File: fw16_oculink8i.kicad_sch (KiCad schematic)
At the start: 18 parts, among them J1 173162-0131, J3 Fan0, J4 Fan1, U1 BR24G32FVT-3GE2

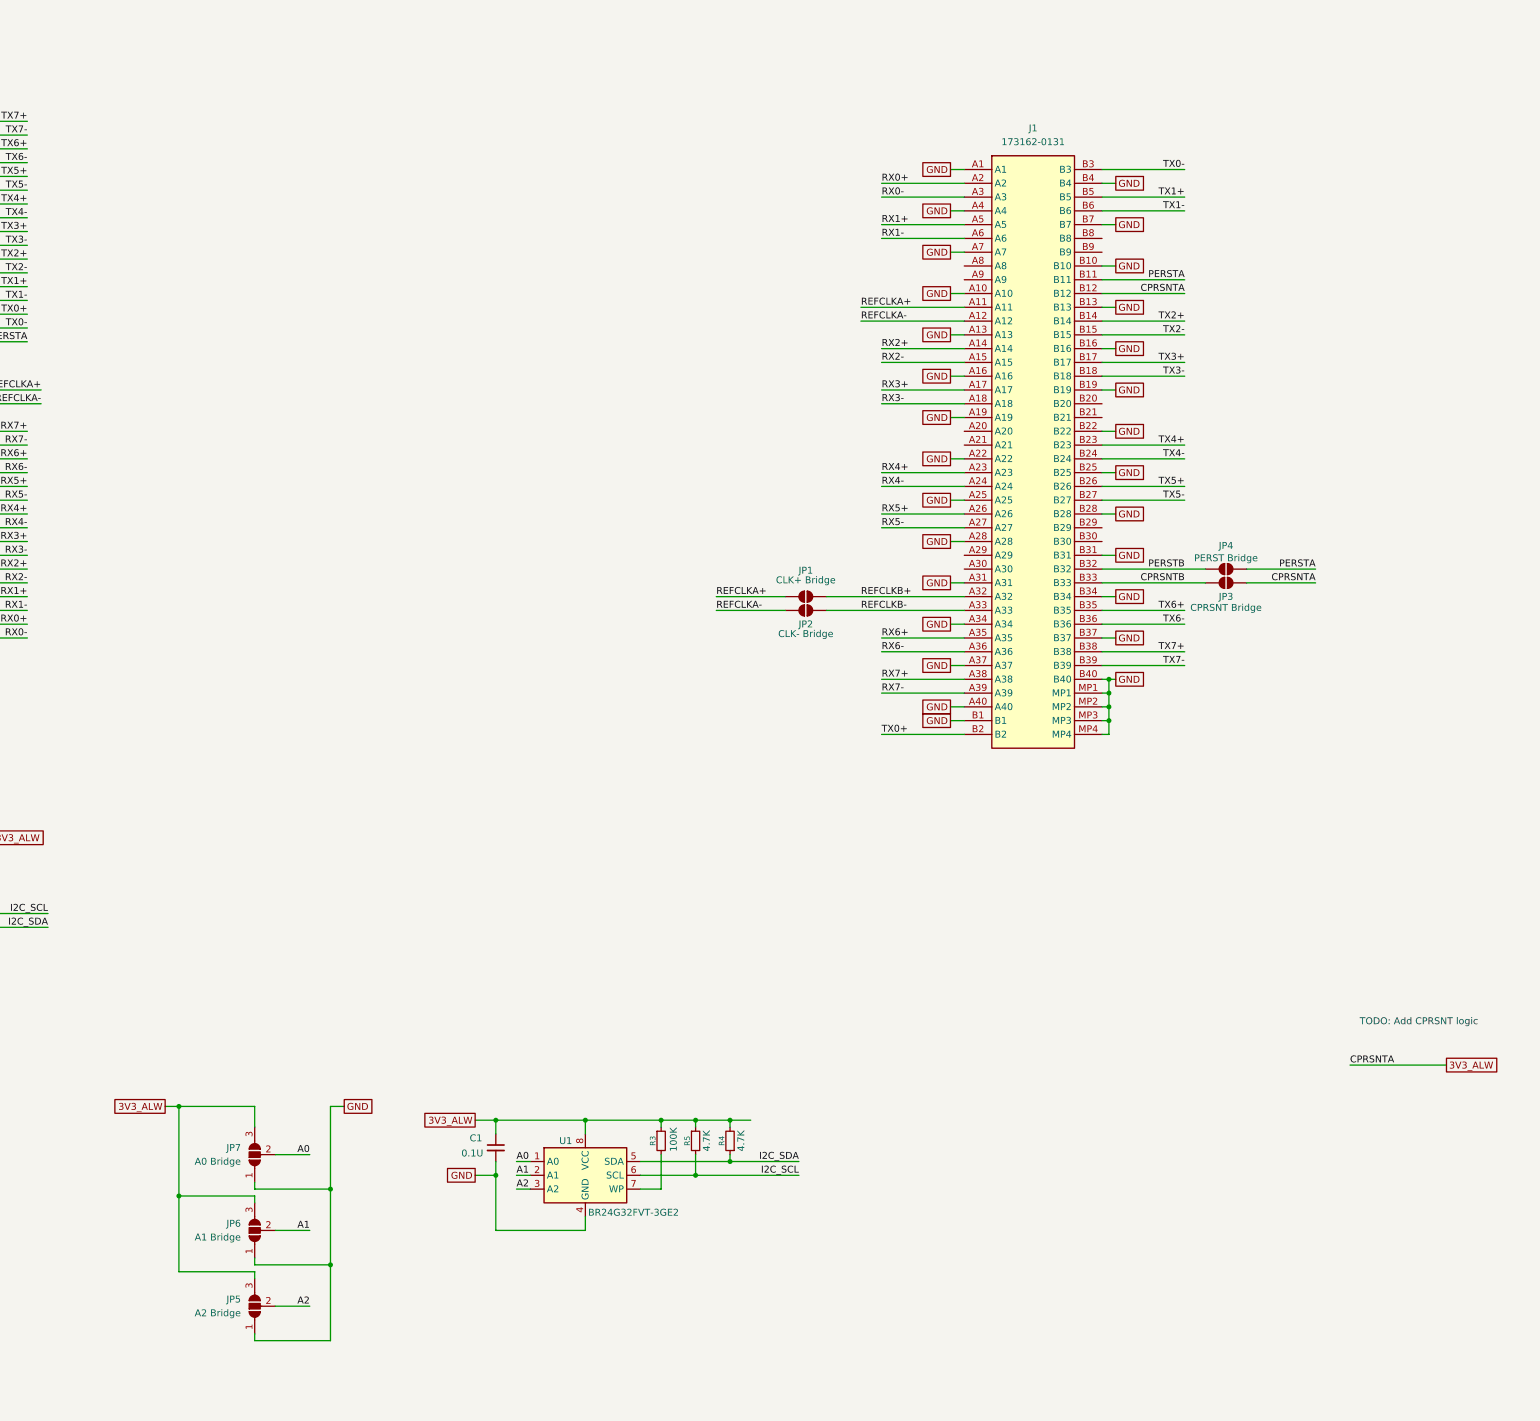
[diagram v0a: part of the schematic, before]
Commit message: Switch to 0R resistor rather than jumper solder pads
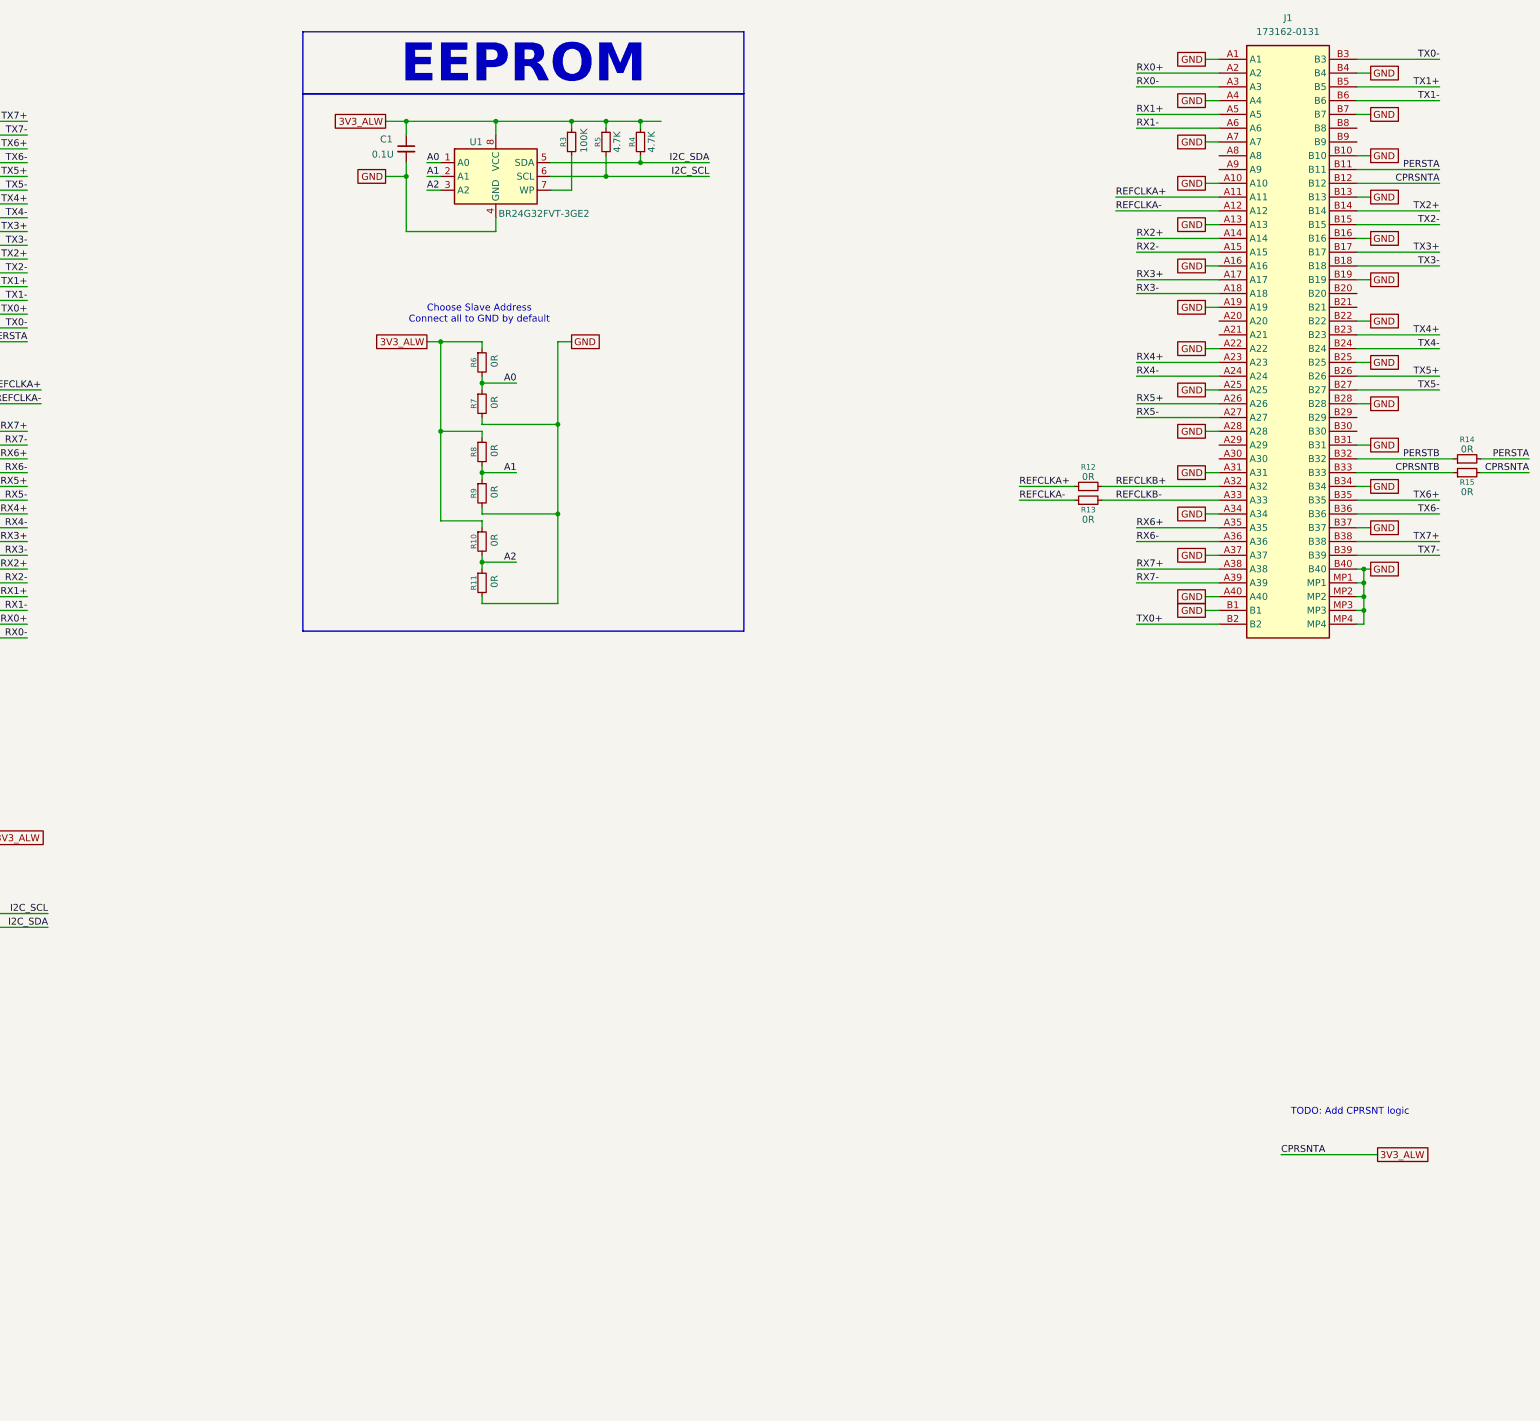
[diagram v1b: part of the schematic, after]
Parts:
- removed JP1: CLK+ Bridge, Jumper:SolderJumper-2_P1.3mm_Open_TrianglePad1.0x1.5mm, symbol Jumper:SolderJumper_2_Open
- removed JP2: CLK- Bridge, Jumper:SolderJumper-2_P1.3mm_Open_TrianglePad1.0x1.5mm, symbol Jumper:SolderJumper_2_Open
- removed JP3: CPRSNT Bridge, Jumper:SolderJumper-2_P1.3mm_Open_TrianglePad1.0x1.5mm, symbol Jumper:SolderJumper_2_Open
- removed JP4: PERST Bridge, Jumper:SolderJumper-2_P1.3mm_Open_TrianglePad1.0x1.5mm, symbol Jumper:SolderJumper_2_Open
- removed JP5: A2 Bridge, Jumper:SolderJumper-3_P1.3mm_Open_Pad1.0x1.5mm, symbol Jumper:SolderJumper_3_Open
- removed JP6: A1 Bridge, Jumper:SolderJumper-3_P1.3mm_Open_Pad1.0x1.5mm, symbol Jumper:SolderJumper_3_Open
- removed JP7: A0 Bridge, Jumper:SolderJumper-3_P1.3mm_Open_Pad1.0x1.5mm, symbol Jumper:SolderJumper_3_Open
- added R10, R11, R12, R13, R14, R15, R6, R7, R8, R9: 0R, Resistor_SMD:R_0402_1005Metric, symbol Device:R_Small
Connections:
- net 3V3_ALW: now also R10.1, R15.2, R6.1, R8.1
- net A0: now also R6.2, R7.1
- net A1: now also R8.2, R9.1
- net A2: now also R10.2, R11.1
- net CPRSNTB: now also R15.1
- net GND: now also R11.2, R7.2, R9.2
- net PERSTA: now also R14.2
- net PERSTB: now also R14.1
- net REFCLKA+: now also R12.1
- net REFCLKA-: now also R13.1
- net REFCLKB+: now also R12.2
- net REFCLKB-: now also R13.2
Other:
- note added: "Choose Slave Address Connect all to GND by default"
- moved on the sheet: C1, J1, R3, R4, R5, U1

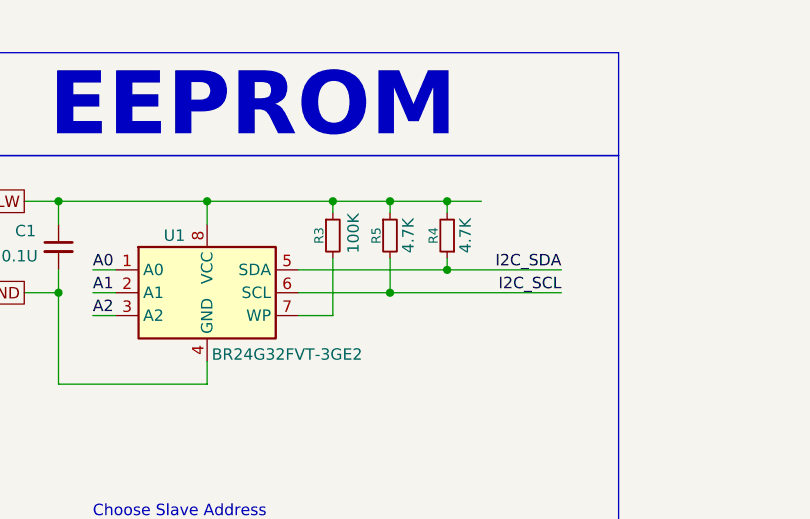
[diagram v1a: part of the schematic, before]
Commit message: Change resistor numbering
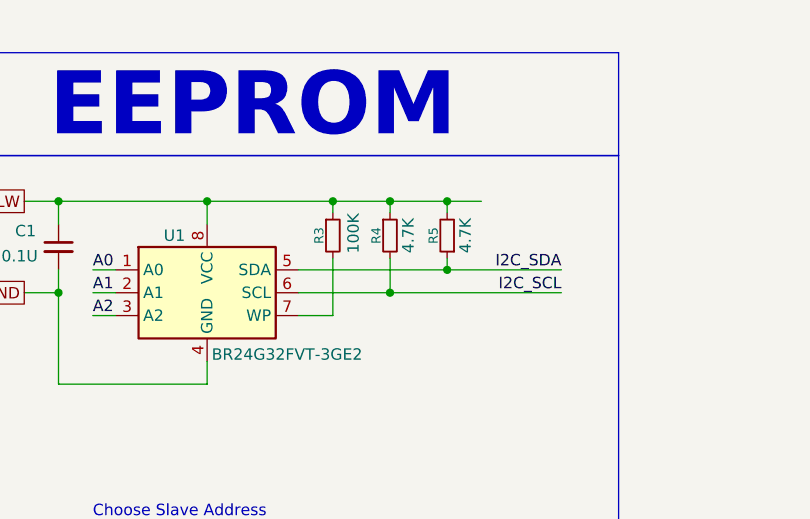
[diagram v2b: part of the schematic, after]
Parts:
- renumbered R5 to R4, R4 to R5
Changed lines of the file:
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@@
 		(on_board yes)
 		(dnp no)
-		(property "Reference" "R5"
+		(property "Reference" "R4"
 			(at 220.726 39.37 90)
 			(effects
@@
 			(project "ExpansionBay to OCuLink 8i (SFF-8612)"
 				(path "/50f5fd03-67f8-43d1-8bfe-dca2cf908bf0"
-					(reference "R5")
+					(reference "R4")
 					(unit 1)
 				)
@@
 		(on_board yes)
 		(dnp no)
-		(property "Reference" "R4"
+		(property "Reference" "R5"
 			(at 227.076 39.37 90)
 			(effects
@@
 			(project "ExpansionBay to OCuLink 8i (SFF-8612)"
 				(path "/50f5fd03-67f8-43d1-8bfe-dca2cf908bf0"
-					(reference "R4")
-					(unit 1)
-				)
+					(reference "R5")
+					(unit 1)
+				)

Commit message: schematic cleanup
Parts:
- J1: renamed from J2; value ~ -> FXBeam
- J3: renamed from J4; Part Nr. (none) -> JUSHUO AFC05-S04FIA-00
- R1, R2: Field5 0402 1% -> (none); Tolerance (none) -> 1%
- R3, R4, R5: Tolerance (none) -> 1%
- renumbered J3 to J2, J1 to J4
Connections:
- net FAN0_SPD: now reaches J1.PH2 (Fan0_SPEED), J2.2 (Pin_2)
- net FAN1_SPD: now reaches J1.PJ2 (Fan1_SPEED), J3.2 (Pin_2)
- net FAN1_PWM: now reaches J1.PK5 (Fan1_PWM), J3.3 (Pin_3)
- net 12V_FAN: now reaches J1.PL4 (12V_FAN), J2.1 (Pin_1), J3.1 (Pin_1)
- net FAN0_PWM: now reaches J1.PL5 (Fan0_PWM), J2.3 (Pin_3)
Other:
- moved on the sheet: C1, J1, J2, J3, J4, R1, R10, R11, R12, R13, R14, R15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
